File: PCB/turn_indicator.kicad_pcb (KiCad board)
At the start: 2 copper layers, 7 parts

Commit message: pcb subfolder and unknown pending changes
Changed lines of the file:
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@@
     )
   )
-  (gr_text "Buttons\n<------" (at 116.84 157.48) (layer F.Cu)
+  (gr_text "Buttons\n<------" (at 99.06 157.48) (layer F.Cu)
     (effects (font (size 1.5 1.5) (thickness 0.3)))
   )
@@
   (segment (start 81.32 134.58) (end 81.32 121.88) (width 1) (layer B.Cu) (net 5))
   (segment (start 81.28 121.84) (end 81.28 116.84) (width 1) (layer B.Cu) (net 5))
-  (segment (start 81.28 116.84) (end 104.14 116.84) (width 1) (layer B.Cu) (net 5))
-  (segment (start 104.14 116.84) (end 104.14 119.38) (width 1) (layer B.Cu) (net 5))
-  (segment (start 104.14 116.84) (end 119.38 116.84) (width 1) (layer B.Cu) (net 5))
-  (segment (start 119.38 116.84) (end 119.38 119.38) (width 1) (layer B.Cu) (net 5))
   (segment (start 81.32 134.58) (end 81.32 149.82) (width 1) (layer B.Cu) (net 5))
   (segment (start 81.32 149.82) (end 81.36 149.86) (width 1) (layer B.Cu) (net 5))
@@
   (segment (start 81.36 149.86) (end 86.36 149.86) (width 1) (layer B.Cu) (net 5))
   (segment (start 86.36 149.86) (end 96.52 149.86) (width 1) (layer B.Cu) (net 5))
+  (segment (start 119.38 116.84) (end 119.38 119.38) (width 1) (layer B.Cu) (net 5))
+  (segment (start 104.14 116.84) (end 104.14 119.38) (width 1) (layer B.Cu) (net 5))
+  (segment (start 104.14 116.84) (end 119.38 116.84) (width 1) (layer B.Cu) (net 5))
+  (segment (start 81.28 116.84) (end 104.14 116.84) (width 1) (layer B.Cu) (net 5))
   (segment (start 121.8 142.36) (end 121.92 142.24) (width 0.5) (layer B.Cu) (net 6))
   (segment (start 121.8 147.32) (end 121.8 142.36) (width 0.5) (layer B.Cu) (net 6))
@@
   (segment (start 119.3 147.32) (end 119.3 142.32) (width 0.5) (layer B.Cu) (net 8))
   (segment (start 83.82 132.08) (end 83.82 124.46) (width 1) (layer B.Cu) (net 9))
-  (segment (start 111.64 124.34) (end 111.64 119.38) (width 1) (layer B.Cu) (net 9))
-  (segment (start 111.76 124.46) (end 111.64 124.34) (width 1) (layer B.Cu) (net 9))
-  (segment (start 111.76 124.46) (end 127 124.46) (width 1) (layer B.Cu) (net 9))
-  (segment (start 126.88 124.34) (end 126.88 119.38) (width 1) (layer B.Cu) (net 9))
-  (segment (start 127 124.46) (end 126.88 124.34) (width 1) (layer B.Cu) (net 9))
   (segment (start 99.06 124.46) (end 99.06 127) (width 1) (layer B.Cu) (net 9))
   (segment (start 83.82 124.46) (end 99.06 124.46) (width 1) (layer B.Cu) (net 9))
   (segment (start 99.06 124.46) (end 111.76 124.46) (width 1) (layer B.Cu) (net 9))
+  (segment (start 127 124.46) (end 126.88 124.34) (width 1) (layer B.Cu) (net 9))
+  (segment (start 126.88 124.34) (end 126.88 119.38) (width 1) (layer B.Cu) (net 9))
+  (segment (start 111.76 124.46) (end 127 124.46) (width 1) (layer B.Cu) (net 9))
+  (segment (start 111.76 124.46) (end 111.64 124.34) (width 1) (layer B.Cu) (net 9))
+  (segment (start 111.64 124.34) (end 111.64 119.38) (width 1) (layer B.Cu) (net 9))
   (segment (start 116.8 142.28) (end 116.84 142.24) (width 0.5) (layer B.Cu) (net 10))
   (segment (start 116.8 147.32) (end 116.8 142.28) (width 0.5) (layer B.Cu) (net 10))
@@
   (segment (start 106.56 142.36) (end 106.68 142.24) (width 0.5) (layer B.Cu) (net 18))
   (segment (start 106.56 147.32) (end 106.56 142.36) (width 0.5) (layer B.Cu) (net 18))
+  (segment (start 106.64 119.38) (end 106.64 121.88) (width 0.5) (layer F.Cu) (net 19))
   (segment (start 106.64 121.88) (end 111.76 127) (width 0.5) (layer F.Cu) (net 19))
-  (segment (start 106.64 119.38) (end 106.64 121.88) (width 0.5) (layer F.Cu) (net 19))
   (segment (start 104.06 142.32) (end 104.14 142.24) (width 0.5) (layer B.Cu) (net 20))
   (segment (start 104.06 147.32) (end 104.06 142.32) (width 0.5) (layer B.Cu) (net 20))
@@
   (segment (start 101.56 142.28) (end 101.6 142.24) (width 0.5) (layer B.Cu) (net 22))
   (segment (start 101.56 147.32) (end 101.56 142.28) (width 0.5) (layer B.Cu) (net 22))
+  (segment (start 121.88 121.96) (end 116.84 127) (width 0.5) (layer F.Cu) (net 23))
   (segment (start 121.88 119.38) (end 121.88 121.96) (width 0.5) (layer F.Cu) (net 23))
-  (segment (start 121.88 121.96) (end 116.84 127) (width 0.5) (layer F.Cu) (net 23))
   (segment (start 124.38 122) (end 119.38 127) (width 0.5) (layer F.Cu) (net 24))
   (segment (start 124.38 119.38) (end 124.38 122) (width 0.5) (layer F.Cu) (net 24))

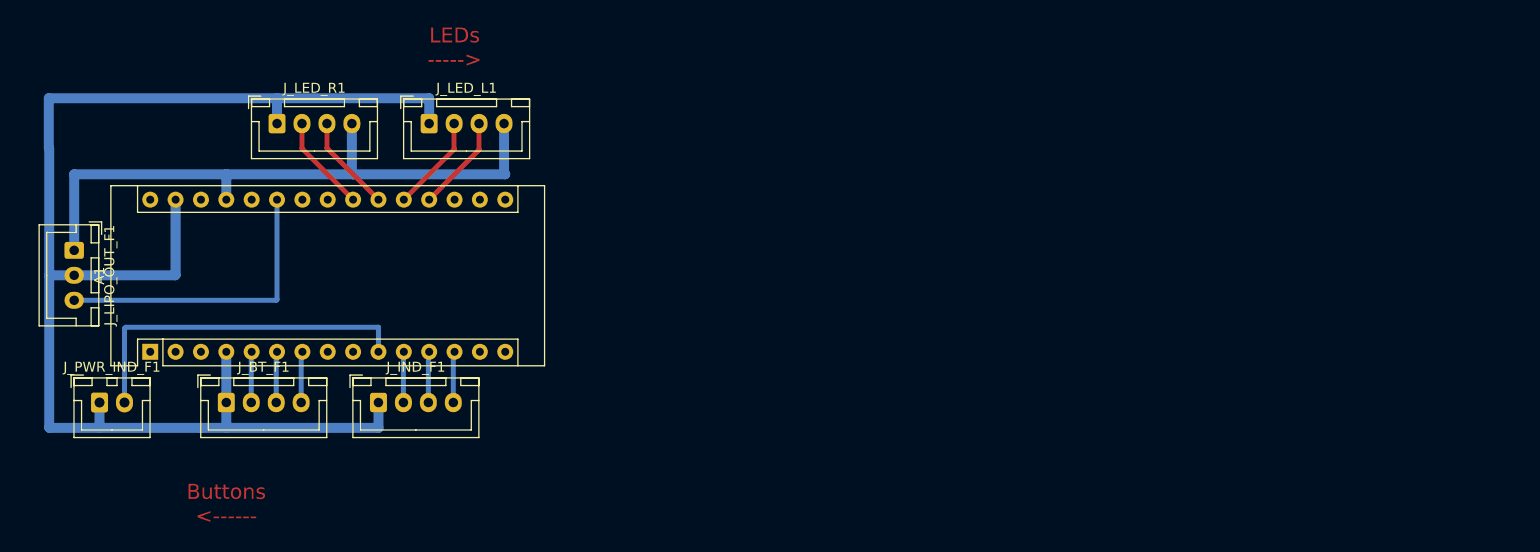
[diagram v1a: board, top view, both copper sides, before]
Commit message: shrink to 5x7 perfboard, add comments, add fuse and capacitors
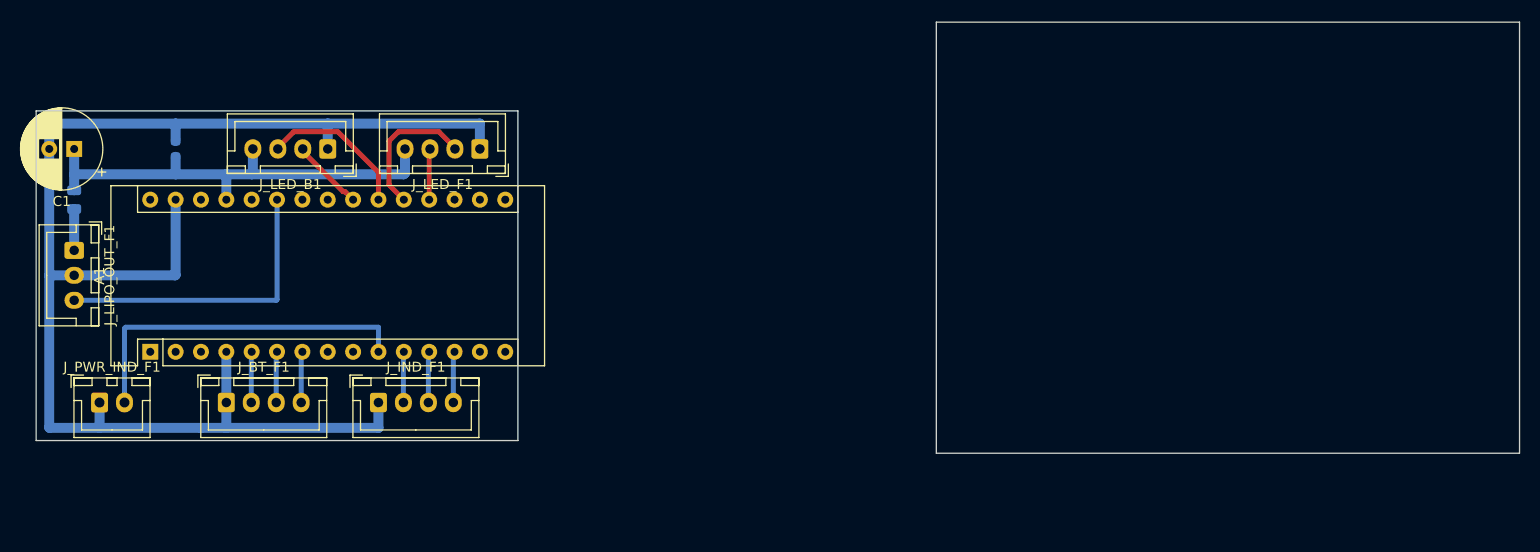
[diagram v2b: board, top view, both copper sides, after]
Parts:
- removed J_LED_L1, J_LED_R1: Conn_01x04_Female, Connector_JST:JST_XH_B4B-XH-A_1x04_P2.50mm_Vertical
- added C1: 200uF, Capacitor_THT:CP_Radial_D8.0mm_P2.50mm, F.Cu at (83.8, 121.9)
- added C2: 100nF, Capacitor_SMD:C_0603_1608Metric, B.Cu at (94.0, 121.9)
- added F1: 0.5A, Fuse:Fuse_0805_2012Metric, B.Cu at (83.8, 127.0)
- added J_LED_B1: Conn_01x04_Female, Connector_JST:JST_XH_B4B-XH-A_1x04_P2.50mm_Vertical, F.Cu at (109.2, 121.9)
- added J_LED_F1: Conn_01x04_Female, Connector_JST:JST_XH_B4B-XH-A_1x04_P2.50mm_Vertical, F.Cu at (124.5, 121.9)
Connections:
- A1 pad 1: Net-(A1-Pad1) -> (no net)
- A1 pad 14: Net-(A1-Pad14) -> (no net)
- A1 pad 15: Net-(A1-Pad15) -> (no net)
- A1 pad 16: Net-(A1-Pad16) -> (no net)
- A1 pad 17: Net-(A1-Pad17) -> (no net)
- A1 pad 18: Net-(A1-Pad18) -> (no net)
- A1 pad 19: DATA_LEDS_L -> DATA_LEDS_F
- A1 pad 2: Net-(A1-Pad2) -> (no net)
- A1 pad 20: CLOCK_LEDS_L -> CLOCK_LEDS_F
- A1 pad 21: DATA_LEDS_R -> DATA_LEDS_B
- A1 pad 22: CLOCK_LEDS_R -> CLOCK_LEDS_B
- A1 pad 23: Net-(A1-Pad23) -> (no net)
- A1 pad 24: Net-(A1-Pad24) -> (no net)
- A1 pad 26: Net-(A1-Pad26) -> (no net)
- A1 pad 28: Net-(A1-Pad28) -> (no net)
- A1 pad 3: Net-(A1-Pad3) -> (no net)
- A1 pad 30: Net-(A1-Pad30) -> (no net)
- A1 pad 8: Net-(A1-Pad8) -> (no net)
- A1 pad 9: Net-(A1-Pad9) -> (no net)
- J_LIPO_OUT_F1 pad 1: +5V -> Net-(F1-Pad1)
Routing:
- net +5V: track 63.6 -> 46.6 mm
- net DATA_LEDS_B: track 0.00 -> 15.3 mm
- net CLOCK_LEDS_F: track 0.00 -> 14.3 mm
- net DATA_LEDS_R: track 9.76 -> 0.00 mm
- net CLOCK_LEDS_R: track 9.74 -> 0.00 mm
- net CLOCK_LEDS_L: track 9.71 -> 0.00 mm
- net DATA_LEDS_L: track 9.69 -> 0.00 mm
- net CLOCK_LEDS_B: track 0.00 -> 7.28 mm
- net DATA_LEDS_F: track 0.00 -> 5.11 mm
- net GND: track 142.1 -> 146.4 mm
- net Net-(F1-Pad1): track 0.00 -> 4.14 mm
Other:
- board outline added: 148.6 x 43.2 mm
- board text added: "<------ Buttons"
- board text added: "routed manually on a 5x7 perfboard. B.Cu is layed as tracks, F.Cu are loose wires"
- board text removed: "Buttons <------"

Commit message: migrate to kicad 6, add gh actions from easylight
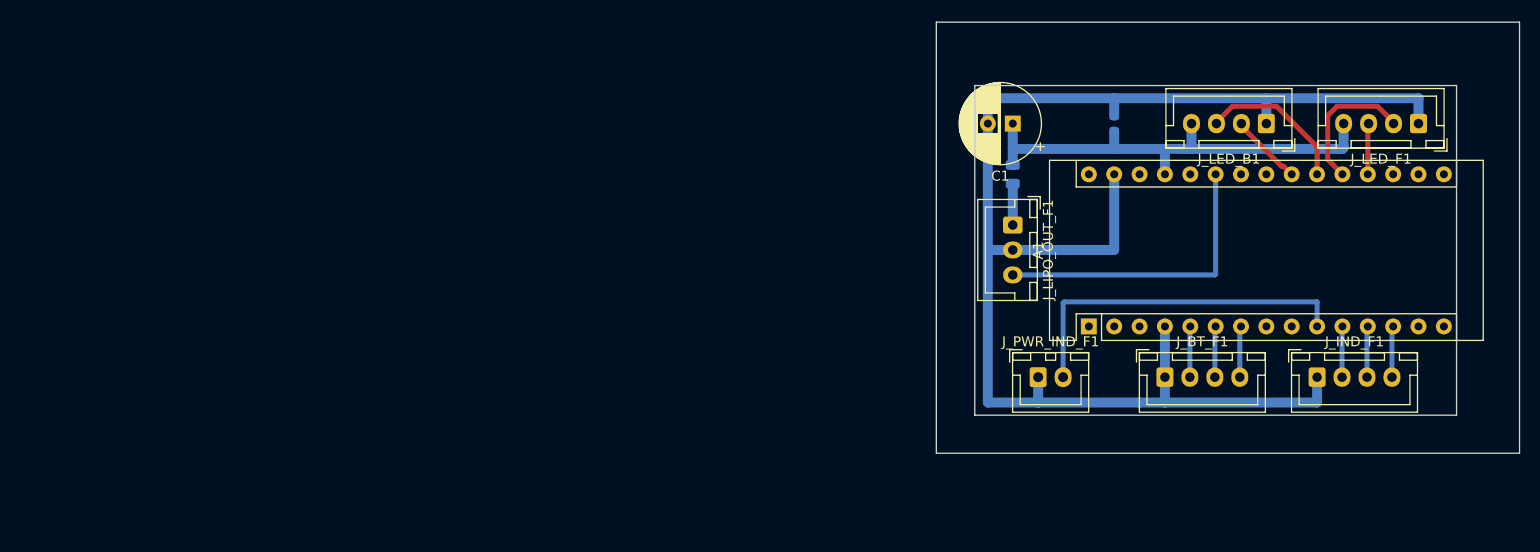
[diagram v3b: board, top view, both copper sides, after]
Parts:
- moved A1 94.1 mm to (185.5, 139.7)
- moved C1 94.1 mm to (177.8, 119.4)
- moved F1 94.1 mm to (177.8, 124.5)
- moved J_BT_F1 94.1 mm to (193.1, 144.8)
- moved J_LED_B1 94.1 mm to (203.2, 119.4)
- moved J_LIPO_OUT_F1 94.1 mm to (177.8, 129.5)
- moved C2 94.1 mm to (188.0, 119.4)
- moved J_IND_F1 94.1 mm to (208.3, 144.8)
- moved J_LED_F1 94.1 mm to (218.5, 119.4)
- moved J_PWR_IND_F1 94.1 mm to (180.4, 144.8)
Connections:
- A1 pad 1: (no net) -> unconnected-(A1-Pad1)
- A1 pad 14: (no net) -> unconnected-(A1-Pad14)
- A1 pad 15: (no net) -> unconnected-(A1-Pad15)
- A1 pad 16: (no net) -> unconnected-(A1-Pad16)
- A1 pad 17: (no net) -> unconnected-(A1-Pad17)
- A1 pad 18: (no net) -> unconnected-(A1-Pad18)
- A1 pad 2: (no net) -> unconnected-(A1-Pad2)
- A1 pad 23: (no net) -> unconnected-(A1-Pad23)
- A1 pad 24: (no net) -> unconnected-(A1-Pad24)
- A1 pad 26: (no net) -> unconnected-(A1-Pad26)
- A1 pad 28: (no net) -> unconnected-(A1-Pad28)
- A1 pad 3: (no net) -> unconnected-(A1-Pad3)
- A1 pad 30: (no net) -> unconnected-(A1-Pad30)
- A1 pad 8: (no net) -> unconnected-(A1-Pad8)
- A1 pad 9: (no net) -> unconnected-(A1-Pad9)
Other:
- board size 148.6 x 43.2 mm -> 58.4 x 43.2 mm
- net class Default removed
- net class PWR removed

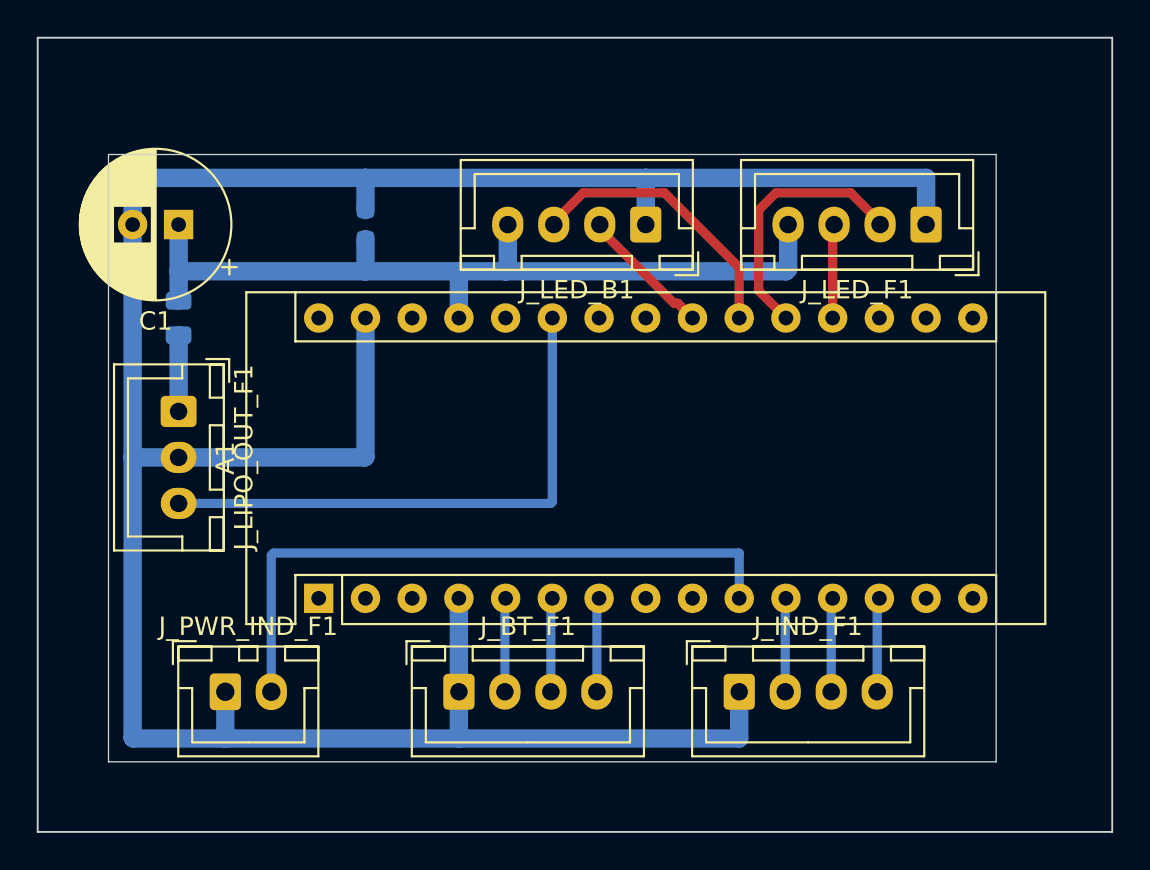
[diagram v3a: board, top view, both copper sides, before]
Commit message: update to kicad 7, increase fuse size to proper 1206, cleanup PCB, include QR code and MF logo
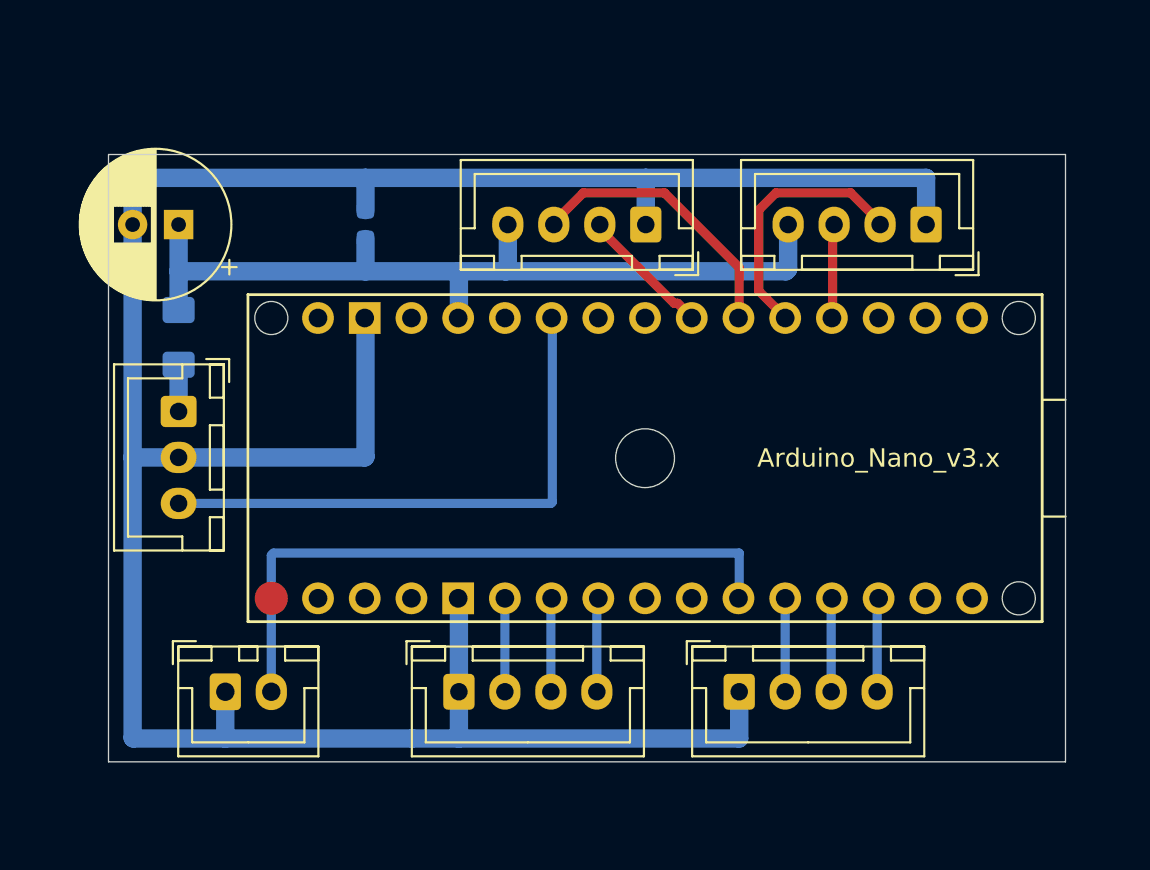
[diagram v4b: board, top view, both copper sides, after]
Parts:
- added H1: MountingHole, MountingHole:MountingHole_3.2mm_M3, F.Cu at (203.2, 132.1)
- A1: footprint Module:Arduino_Nano -> PCM_arduino-library:Arduino_Nano_Socket
- F1: footprint Fuse:Fuse_0805_2012Metric -> Fuse:Fuse_1206_3216Metric_Pad1.42x1.75mm_HandSolder
- J_BT_F1, J_IND_F1, J_LED_B1, J_LED_F1: value Conn_01x04_Female -> Conn_01x04_Socket
- J_LIPO_OUT_F1: value Conn_01x03_Female -> Conn_01x03_Socket
- J_PWR_IND_F1: value Conn_01x02_Female -> Conn_01x02_Socket
- moved A1 40.1 mm to (224.8, 132.1)
- moved F1 1.05 mm to (177.8, 125.5)
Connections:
- J_BT_F1 pad 2: BT_L -> BT_LEFT
- J_IND_F1 pad 2: BT_L_IND -> BT_LEFT_IND
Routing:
- net BT_L_IND: track 5.10 -> 0.00 mm
- net BT_LEFT_IND: track 0.00 -> 5.10 mm
- net BT_LEFT: track 0.00 -> 5.10 mm
- net BT_L: track 5.10 -> 0.00 mm
- net Net-(J_LIPO_OUT_F1-Pin_1): track 4.14 -> 2.54 mm
- net +5V: track 46.6 -> 47.1 mm
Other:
- board size 58.4 x 43.2 mm -> 52 x 33 mm
